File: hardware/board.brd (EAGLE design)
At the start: 53 x 30 mm, 45 parts, among them IC1 0915BM15A0001, J1 U.FL, U3 BLE113-A, X1 26MHz 10pF 10ppm -20C +70C, X3 MINI-USB-UX60-MB-5ST

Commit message: Update parts for 24MHz in schematic and BOM
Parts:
- C5, C6: value 27pF -> 11pF
- X1: value 26MHz 10pF 10ppm -20C +70C -> 24MHz 8pF 10ppm -20C +70C
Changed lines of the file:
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@@
 <?xml version="1.0" encoding="utf-8"?>
 <!DOCTYPE eagle SYSTEM "eagle.dtd">
-<eagle version="7.1.0">
+<eagle version="7.4.0">
 <drawing>
 <settings>
@@
 <attribute name="VALUE" x="27.43" y="21.405" size="1.016" layer="27" rot="R180"/>
 </element>
-<element name="C5" library="rcl" package="C0402K" value="27pF" x="18.585" y="16.835" smashed="yes" rot="R180">
+<element name="C5" library="rcl" package="C0402K" value="11pF" x="18.585" y="16.835" smashed="yes" rot="R180">
 <attribute name="VALUE" x="19.085" y="18.285" size="1.016" layer="27" rot="R180"/>
 </element>
-<element name="C6" library="rcl" package="C0402K" value="27pF" x="15.255" y="14.585" smashed="yes" rot="R90">
+<element name="C6" library="rcl" package="C0402K" value="11pF" x="15.255" y="14.585" smashed="yes" rot="R90">
 <attribute name="VALUE" x="16.705" y="14.085" size="1.016" layer="27" rot="R90"/>
 </element>
@@
 <attribute name="VALUE" x="38.57" y="12.825" size="1.016" layer="27" rot="SR0"/>
 </element>
-<element name="X1" library="cts_crystal" package="CTS_32X25" value="26MHz 10pF 10ppm -20C +70C" x="17.985" y="14.645" smashed="yes">
+<element name="X1" library="cts_crystal" package="CTS_32X25" value="24MHz 8pF 10ppm -20C +70C" x="17.985" y="14.645" smashed="yes">
 <attribute name="VALUE" x="16.285" y="12.545" size="0.75" layer="27"/>
 </element>

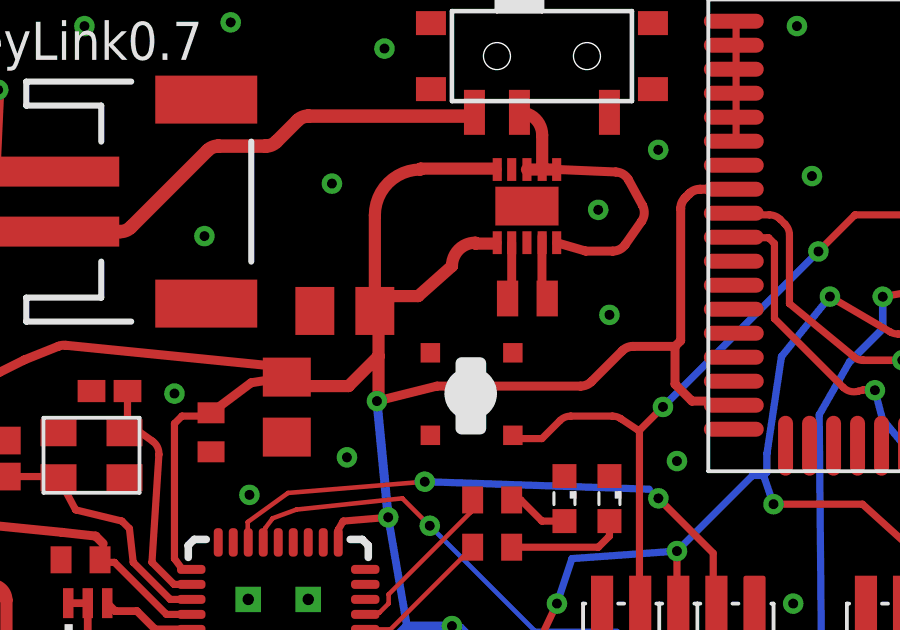
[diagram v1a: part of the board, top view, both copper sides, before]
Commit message: Update loading cap specifications to 12pF
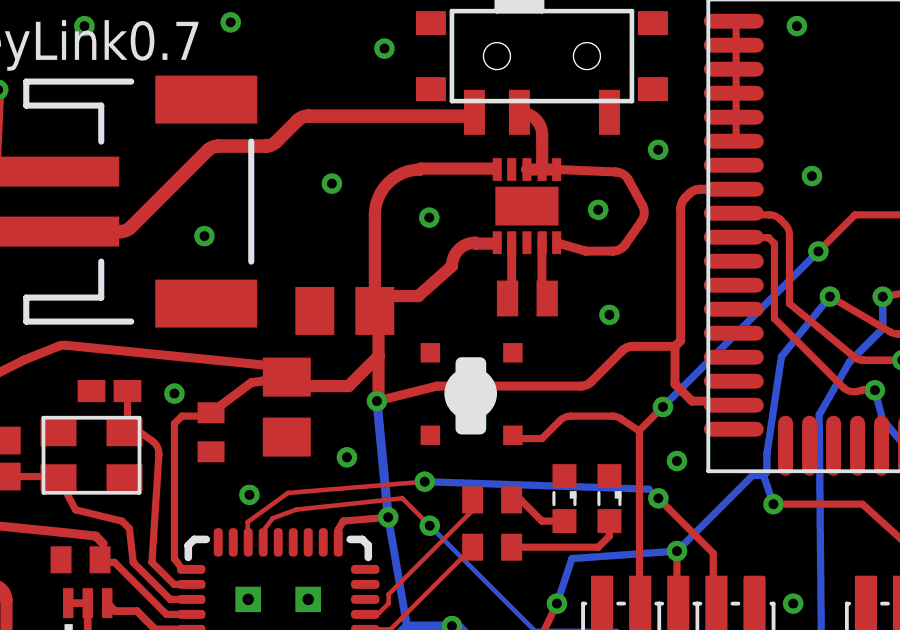
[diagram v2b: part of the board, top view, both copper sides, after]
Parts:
- C5, C6: value 11pF -> 12pF ±5%
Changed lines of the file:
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@@
 <attribute name="VALUE" x="27.43" y="21.405" size="1.016" layer="27" rot="R180"/>
 </element>
-<element name="C5" library="rcl" package="C0402K" value="11pF" x="18.585" y="16.835" smashed="yes" rot="R180">
+<element name="C5" library="rcl" package="C0402K" value="12pF ±5%" x="18.585" y="16.835" smashed="yes" rot="R180">
 <attribute name="VALUE" x="19.085" y="18.285" size="1.016" layer="27" rot="R180"/>
 </element>
-<element name="C6" library="rcl" package="C0402K" value="11pF" x="15.255" y="14.585" smashed="yes" rot="R90">
+<element name="C6" library="rcl" package="C0402K" value="12pF ±5%" x="15.255" y="14.585" smashed="yes" rot="R90">
 <attribute name="VALUE" x="16.705" y="14.085" size="1.016" layer="27" rot="R90"/>
 </element>
@@
 <via x="23.25" y="13.375" extent="1-16" drill="0.3302" diameter="0.4064"/>
 <via x="26.5" y="14.625" extent="1-16" drill="0.3302" diameter="0.4064"/>
-<via x="30.625" y="16.125" extent="1-16" drill="0.3302" diameter="0.4064"/>
+<via x="29.245" y="22.615" extent="1-16" drill="0.3302" diameter="0.4064"/>
 </signal>
 <signal name="VDD">

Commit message: Fix decoupling cap; it was an error to have it so big. Also, the Digikey BOM had a mistake for its part number.
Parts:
- C11: value 100uF -> 10uF
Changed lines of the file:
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@@
 <setting verticaltext="up"/>
 </settings>
-<grid distance="39.3700787" unitdist="mil" unit="mil" style="lines" multiple="1" display="yes" altdistance="0.01" altunitdist="mm" altunit="mm"/>
+<grid distance="0.0393700787" unitdist="inch" unit="inch" style="lines" multiple="1" display="yes" altdistance="0.000393700787" altunitdist="inch" altunit="inch"/>
 <layers>
 <layer number="1" name="Top" color="4" fill="1" visible="yes" active="yes"/>
@@
 <layer number="29" name="tStop" color="7" fill="3" visible="no" active="yes"/>
 <layer number="30" name="bStop" color="7" fill="6" visible="no" active="yes"/>
-<layer number="31" name="tCream" color="7" fill="4" visible="no" active="yes"/>
+<layer number="31" name="tCream" color="7" fill="4" visible="yes" active="yes"/>
 <layer number="32" name="bCream" color="7" fill="5" visible="no" active="yes"/>
 <layer number="33" name="tFinish" color="6" fill="3" visible="no" active="yes"/>
@@
 <attribute name="VALUE" x="17.895" y="6.135" size="1.27" layer="27" rot="R270"/>
 </element>
-<element name="C11" library="rcl" package="C0805K" value="100uF" x="24.495" y="16.3" smashed="yes" rot="R270">
+<element name="C11" library="rcl" package="C0805K" value="10uF" x="24.495" y="16.3" smashed="yes" rot="R270">
 <attribute name="VALUE" x="22.59" y="16.935" size="1.27" layer="27" rot="R270"/>
 </element>

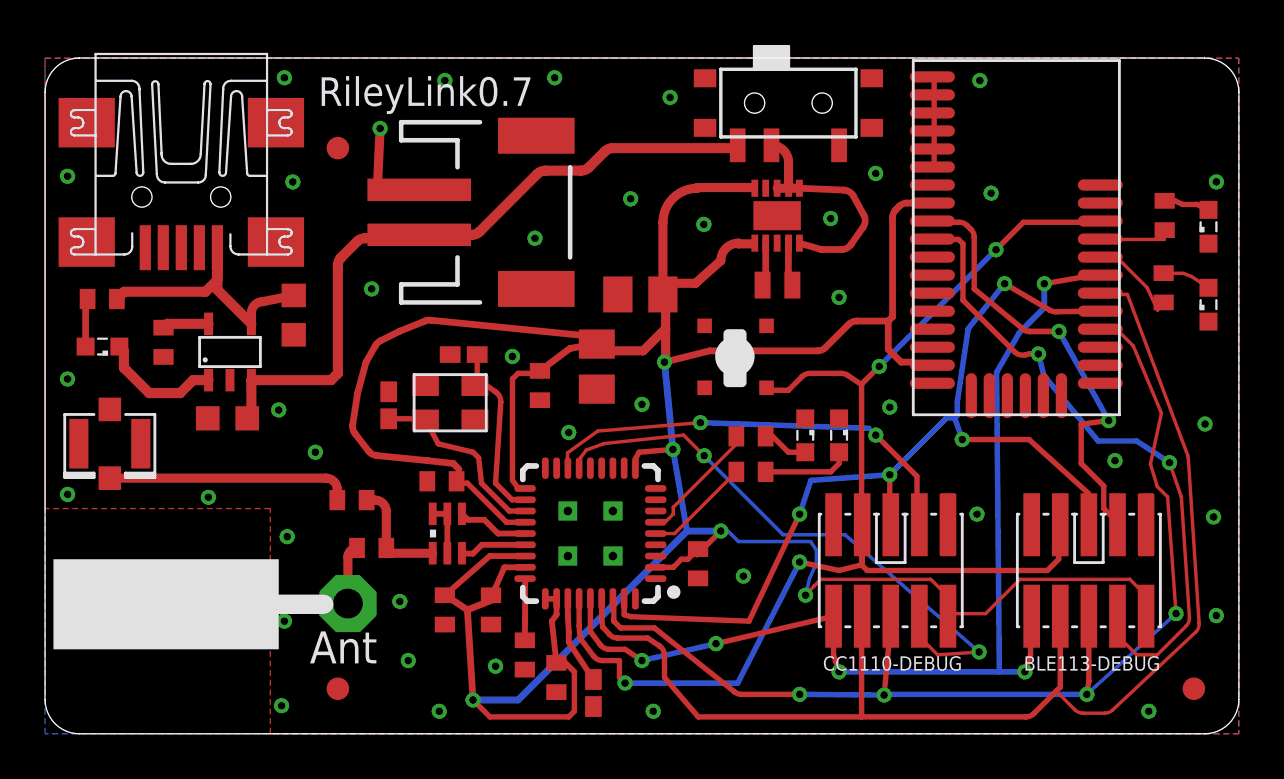
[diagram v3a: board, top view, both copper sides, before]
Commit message: reduce amount of solder under cc1110, and label board 0.7p for production run
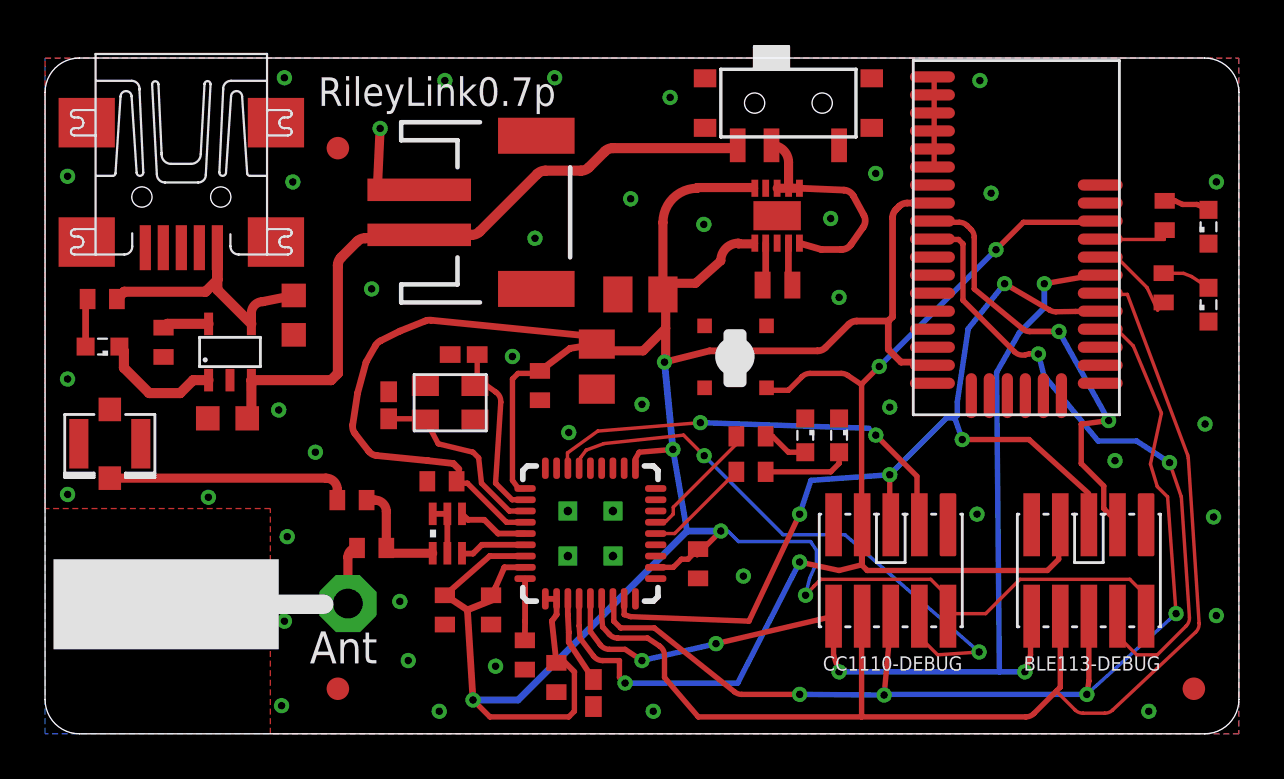
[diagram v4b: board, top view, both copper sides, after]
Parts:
- CC1110: device parts:QLP-36_UPDATE -> board:QLP-36_UPDATE
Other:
- board text added: "RileyLink0.7p"
- board text removed: "RileyLink0.7"
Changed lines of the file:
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@@
 <layer number="24" name="bOrigins" color="15" fill="1" visible="yes" active="yes"/>
 <layer number="25" name="tNames" color="7" fill="1" visible="yes" active="yes"/>
-<layer number="26" name="bNames" color="7" fill="1" visible="no" active="yes"/>
+<layer number="26" name="bNames" color="7" fill="1" visible="yes" active="yes"/>
 <layer number="27" name="tValues" color="7" fill="1" visible="no" active="yes"/>
-<layer number="28" name="bValues" color="7" fill="1" visible="no" active="yes"/>
-<layer number="29" name="tStop" color="7" fill="3" visible="no" active="yes"/>
+<layer number="28" name="bValues" color="7" fill="1" visible="yes" active="yes"/>
+<layer number="29" name="tStop" color="7" fill="3" visible="yes" active="yes"/>
 <layer number="30" name="bStop" color="7" fill="6" visible="no" active="yes"/>
 <layer number="31" name="tCream" color="7" fill="4" visible="yes" active="yes"/>
@@
 <wire x1="51.476" y1="30" x2="1.524" y2="30" width="0" layer="20"/>
 <wire x1="1.524" y1="30" x2="0" y2="28.476" width="0" layer="20" curve="90"/>
-<text x="12.125" y="27.875" size="1.27" layer="25">RileyLink0.7</text>
+<text x="12.125" y="27.875" size="1.27" layer="25">RileyLink0.7p</text>
 <text x="11.75" y="3.125" size="1.4224" layer="25">Ant</text>
 <wire x1="12.375" y1="5.75" x2="10.375" y2="5.75" width="0.8636" layer="21"/>
@@
 <attribute name="VALUE" x="25.795" y="1.31" size="1.016" layer="27" rot="R90"/>
 </element>
-<element name="CC1110" library="parts" package="QLP-36_UPDATE" value="CC1110" x="24.21" y="8.89" smashed="yes" rot="R180">
+<element name="CC1110" library="board" package="QLP-36_UPDATE" value="CC1110" x="24.21" y="8.89" smashed="yes" rot="R180">
 <attribute name="VALUE" x="28.02" y="15.24" size="1.27" layer="27" rot="R180"/>
 </element>

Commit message: Map all parts to digikey part numbers, unify part names and descriptions.
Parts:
- C1, C10, C12, C13, C7, C8: value 100nF -> 0.1uF
- renumbered CHARGER to U1
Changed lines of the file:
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@@
 <attribute name="VALUE" x="49.515" y="11.695" size="0.635" layer="27" font="vector" ratio="16" rot="R180"/>
 </element>
-<element name="C1" library="rcl" package="C0402" value="100nF" x="28.99" y="7.55" smashed="yes" rot="R270">
+<element name="C1" library="rcl" package="C0402" value="0.1uF" x="28.99" y="7.55" smashed="yes" rot="R270">
 <attribute name="VALUE" x="27.085" y="8.185" size="1.27" layer="27" rot="R270"/>
 </element>
-<element name="C10" library="rcl" package="C0402" value="100nF" x="19.8" y="5.5" smashed="yes" rot="R270">
+<element name="C10" library="rcl" package="C0402" value="0.1uF" x="19.8" y="5.5" smashed="yes" rot="R270">
 <attribute name="VALUE" x="17.895" y="6.135" size="1.27" layer="27" rot="R270"/>
 </element>
@@
 <attribute name="VALUE" x="22.59" y="16.935" size="1.27" layer="27" rot="R270"/>
 </element>
-<element name="C12" library="rcl" package="C0402" value="100nF" x="21.97" y="15.46" smashed="yes" rot="R270">
+<element name="C12" library="rcl" package="C0402" value="0.1uF" x="21.97" y="15.46" smashed="yes" rot="R270">
 <attribute name="VALUE" x="20.065" y="16.095" size="1.27" layer="27" rot="R270"/>
 </element>
-<element name="C13" library="rcl" package="C0402" value="100nF" x="17.62" y="11.21" smashed="yes" rot="R180">
+<element name="C13" library="rcl" package="C0402" value="0.1uF" x="17.62" y="11.21" smashed="yes" rot="R180">
 <attribute name="VALUE" x="18.255" y="13.115" size="1.27" layer="27" rot="R180"/>
 </element>
@@
 <attribute name="VALUE" x="16.705" y="14.085" size="1.016" layer="27" rot="R90"/>
 </element>
-<element name="C7" library="rcl" package="C0402" value="100nF" x="22.7" y="2.5" smashed="yes" rot="R270">
+<element name="C7" library="rcl" package="C0402" value="0.1uF" x="22.7" y="2.5" smashed="yes" rot="R270">
 <attribute name="VALUE" x="20.795" y="3.135" size="1.27" layer="27" rot="R270"/>
 </element>
-<element name="C8" library="rcl" package="C0402" value="100nF" x="17.75" y="5.5" smashed="yes" rot="R270">
+<element name="C8" library="rcl" package="C0402" value="0.1uF" x="17.75" y="5.5" smashed="yes" rot="R270">
 <attribute name="VALUE" x="15.845" y="6.135" size="1.27" layer="27" rot="R270"/>
 </element>
@@
 </element>
 <element name="U$2" library="parts" package="PTS540" value="TACTILE_SWITCH" x="30.655" y="16.735" smashed="yes" rot="R270"/>
-<element name="CHARGER" library="parts" package="5PIN_SOT23" value="" x="6.86" y="16.33" smashed="yes">
+<element name="U1" library="parts" package="5PIN_SOT23" value="" x="6.86" y="16.33" smashed="yes">
 <attribute name="VALUE" x="9.4" y="16.33" size="0.4064" layer="27"/>
 </element>
@@
 <contactref element="R1" pad="1"/>
 <contactref element="C2" pad="2"/>
-<contactref element="CHARGER" pad="P$2"/>
+<contactref element="U1" pad="P$2"/>
 <contactref element="C3" pad="2"/>
 <contactref element="JP1" pad="1"/>
@@
 </signal>
 <signal name="N$3">
-<contactref element="CHARGER" pad="P$5"/>
+<contactref element="U1" pad="P$5"/>
 <contactref element="R1" pad="2"/>
 <wire x1="7.26" y1="18.2" x2="5.43" y2="18.2" width="0.45" layer="1"/>
@@
 </signal>
 <signal name="N$2">
-<contactref element="CHARGER" pad="P$1"/>
+<contactref element="U1" pad="P$1"/>
 <contactref element="LED1" pad="C"/>
 <wire x1="7.26" y1="15.7" x2="6.575" y2="15.7" width="0.45" layer="1"/>
@@
 </signal>
 <signal name="VIN_USB">
-<contactref element="CHARGER" pad="P$4"/>
+<contactref element="U1" pad="P$4"/>
 <contactref element="C2" pad="1"/>
 <contactref element="X3" pad="1"/>
@@
 </signal>
 <signal name="VBAT">
-<contactref element="CHARGER" pad="P$3"/>
+<contactref element="U1" pad="P$3"/>
 <contactref element="C3" pad="1"/>
 <contactref element="JP1" pad="2"/>

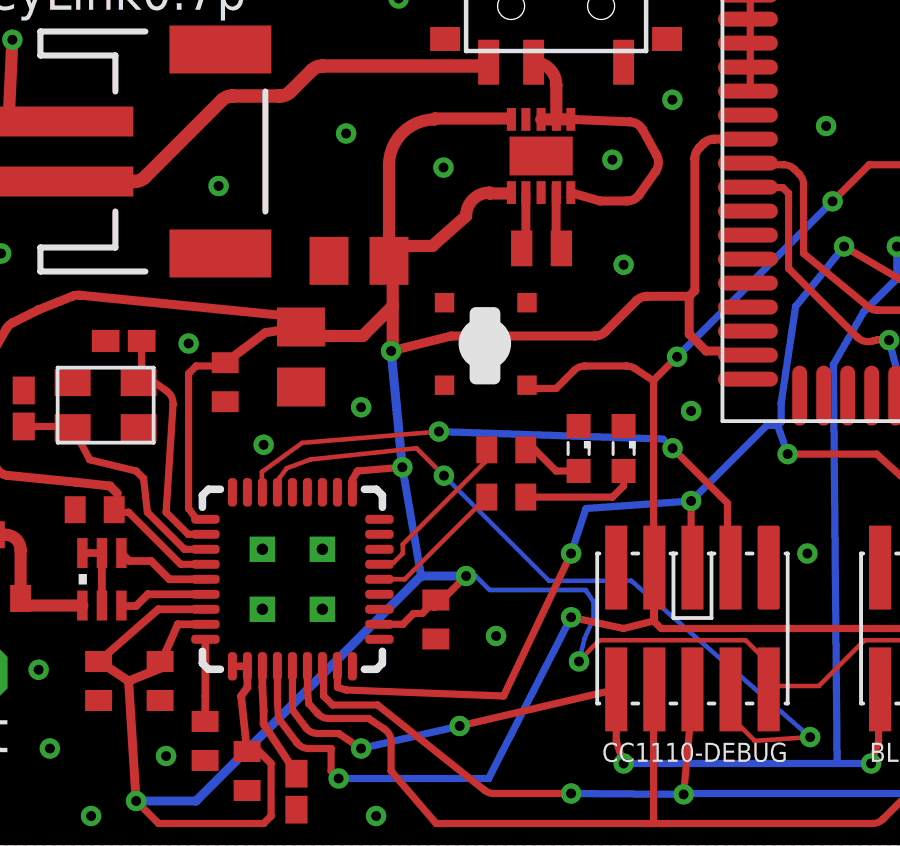
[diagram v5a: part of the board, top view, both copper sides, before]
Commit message: Update placement marks to show part orientation
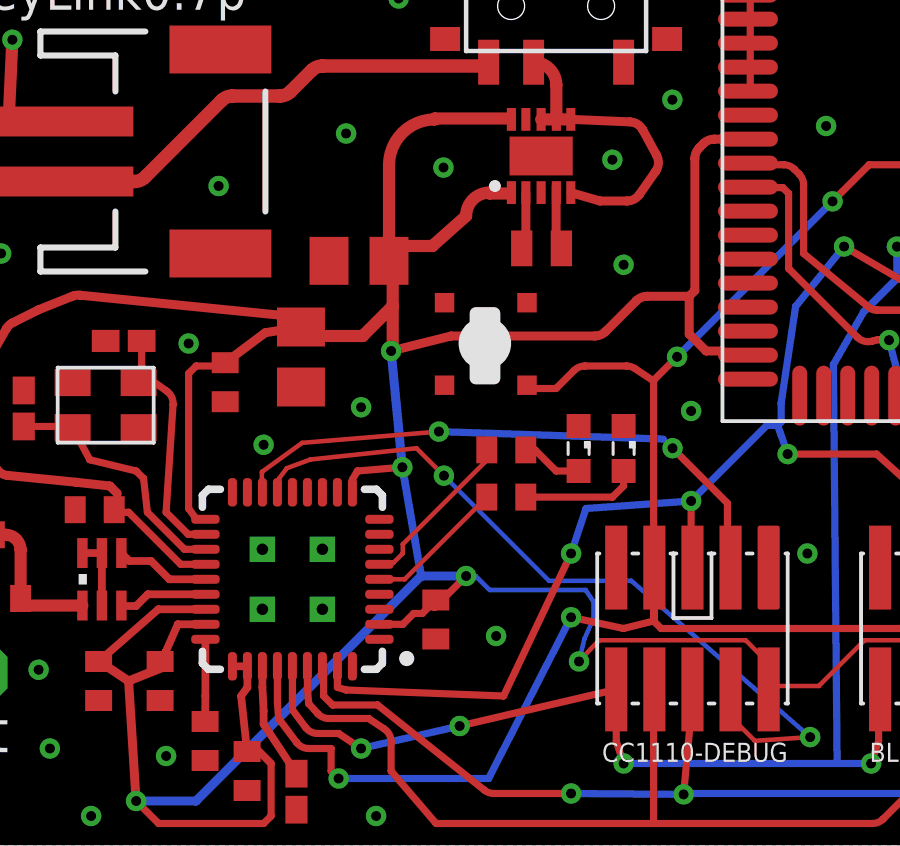
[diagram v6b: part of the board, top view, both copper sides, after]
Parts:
- REGULATOR: device Texas Instruments_By_element14_Batch_1:SON50P260X260X80-11N -> board:SON50P260X260X80-11N
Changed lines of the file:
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@@
 <setting verticaltext="up"/>
 </settings>
-<grid distance="0.0393700787" unitdist="inch" unit="inch" style="lines" multiple="1" display="yes" altdistance="0.000393700787" altunitdist="inch" altunit="inch"/>
+<grid distance="0.1" unitdist="mm" unit="mm" style="lines" multiple="1" display="yes" altdistance="0.000393700787" altunitdist="inch" altunit="inch"/>
 <layers>
 <layer number="1" name="Top" color="4" fill="1" visible="yes" active="yes"/>
@@
 <layer number="49" name="Reference" color="7" fill="1" visible="no" active="yes"/>
 <layer number="50" name="dxf" color="7" fill="1" visible="no" active="no"/>
-<layer number="51" name="tDocu" color="7" fill="1" visible="no" active="yes"/>
+<layer number="51" name="tDocu" color="7" fill="1" visible="yes" active="yes"/>
 <layer number="52" name="bDocu" color="7" fill="1" visible="no" active="yes"/>
 <layer number="53" name="tGND_GNDA" color="7" fill="9" visible="no" active="no"/>
@@
 <attribute name="VALUE" x="9.4" y="16.33" size="0.4064" layer="27"/>
 </element>
-<element name="REGULATOR" library="Texas Instruments_By_element14_Batch_1" package="SON50P260X260X80-11N" value="TPS63031" x="32.5" y="23" smashed="yes" rot="R90">
+<element name="REGULATOR" library="board" package="SON50P260X260X80-11N" value="TPS63031" x="32.5" y="23" smashed="yes" rot="R90">
 <attribute name="PACKAGE" value="SON-10" x="32.5" y="23" size="1.778" layer="27" rot="R90" display="off"/>
 <attribute name="OC_NEWARK" value="19P7478" x="32.5" y="23" size="1.778" layer="27" rot="R90" display="off"/>
